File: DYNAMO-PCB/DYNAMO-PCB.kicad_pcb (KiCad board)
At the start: 2 copper layers, 39 parts, among them J1 HDMI_A, J10 Conn_01x03_Pin, J11 Conn_01x03_Pin, J12 Conn_01x03_Pin, J13 Conn_01x02_Pin, J17 USB3_A, J18 USB3_A, J19 USB3_A, J2 USB3_A, J20 USB3_A, J21 USB3_A, J22 USB3_A, J23 USB3_A, J24 USB3_A, J25 USB3_A, J26 USB_C_Receptacle_USB2.0_16P, J27 USB_C_Receptacle_USB2.0_16P, J28 USB_C_Receptacle_USB2.0_16P, J29 USB_C_Receptacle_USB2.0_16P, J3 Conn_01x03_Pin, J30 USB_C_Receptacle_USB2.0_16P, J31 USB_C_Receptacle_USB2.0_16P, J5 Conn_01x02_Pin, J6 Conn_01x03_Pin, J7 Conn_01x08_Socket, J8 Conn_01x03_Pin, J9 Conn_01x03_Pin, U2 CH7035B-BF

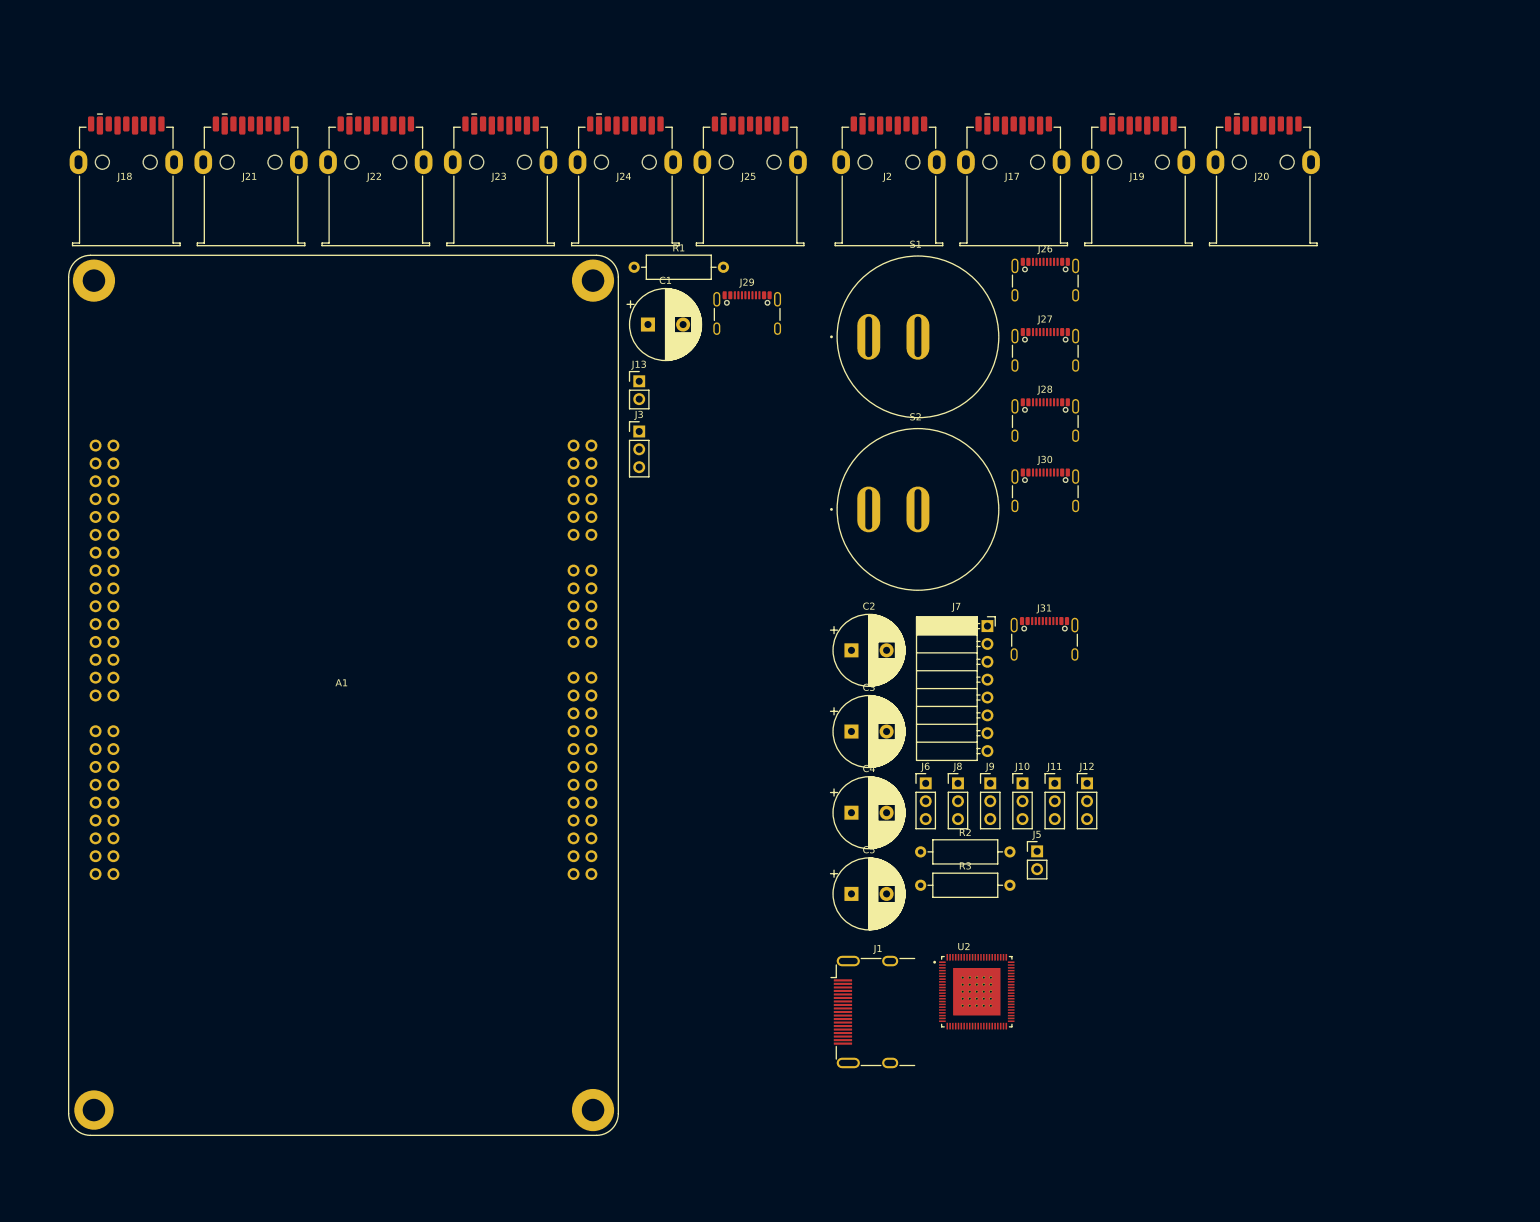
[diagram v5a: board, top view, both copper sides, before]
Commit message: wired headpcb sch
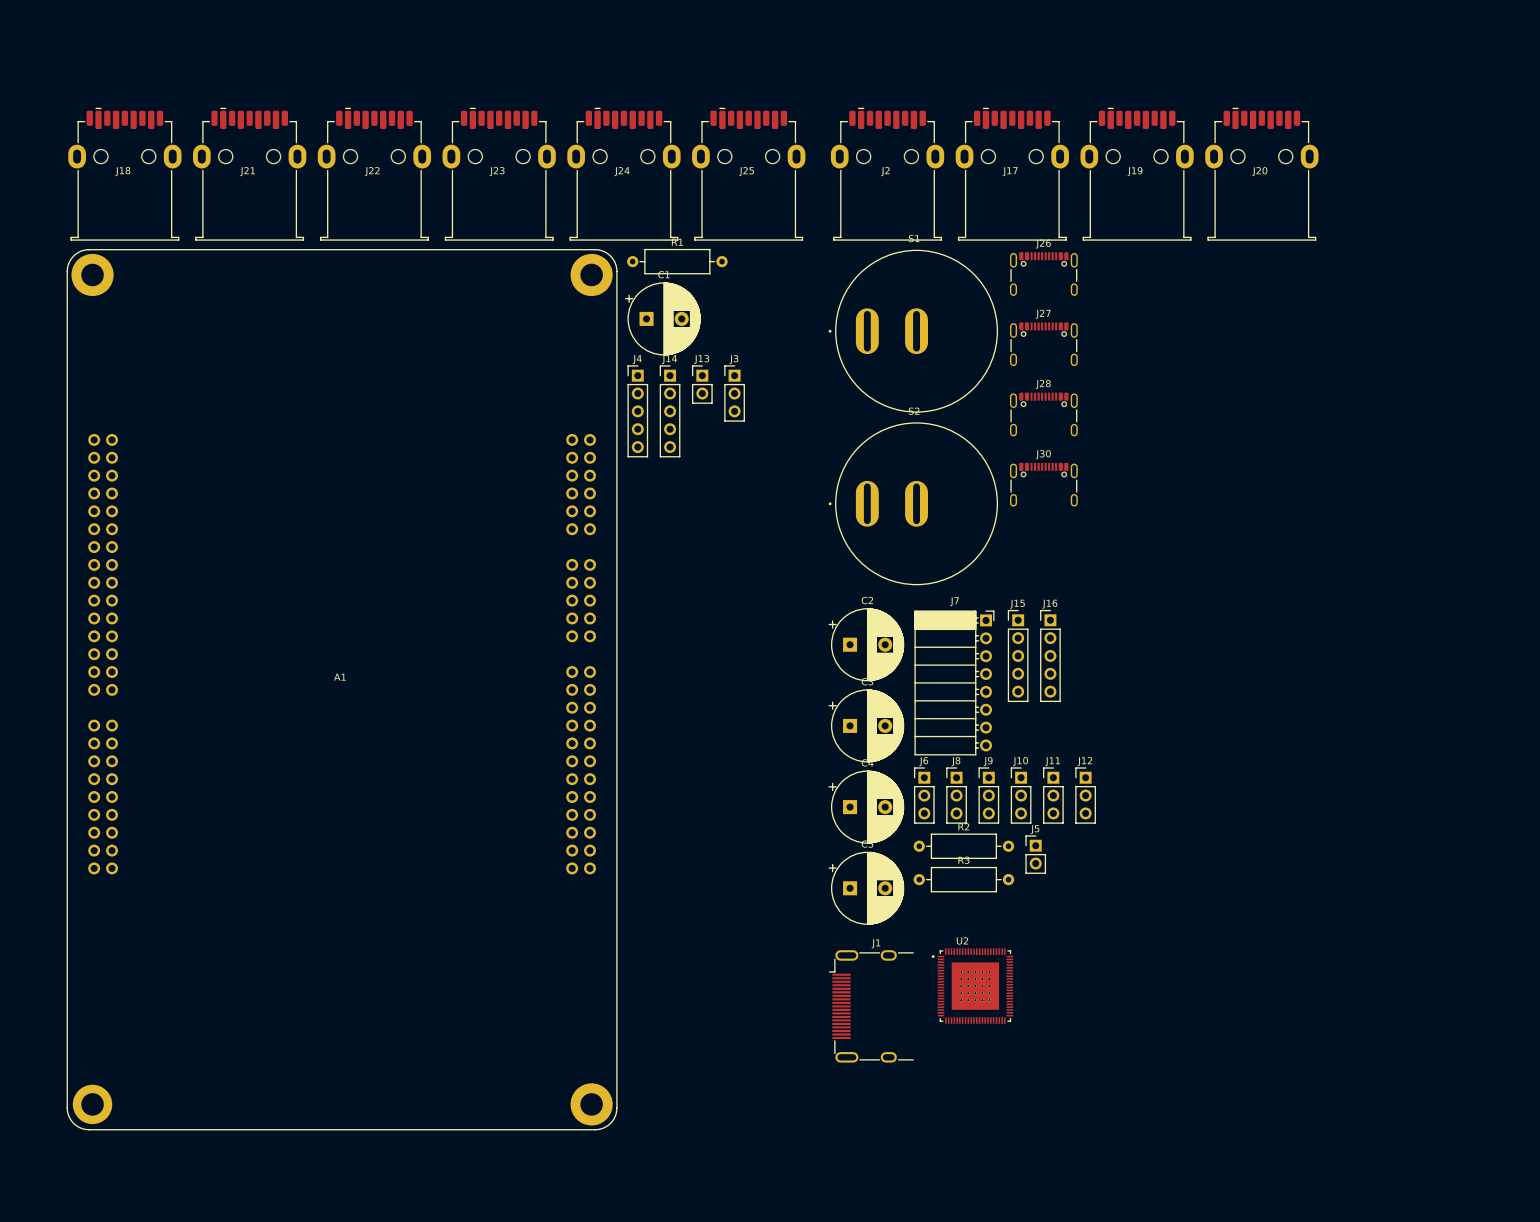
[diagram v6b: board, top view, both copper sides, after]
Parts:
- removed J29, J31: USB_C_Receptacle_USB2.0_16P, Connector_USB:USB_C_Receptacle_GCT_USB4105-xx-A_16P_TopMnt_Horizontal
- added J14: Conn_01x05_Pin, Connector_PinHeader_2.54mm:PinHeader_1x05_P2.54mm_Vertical, F.Cu at (137.8, 65.8)
- added J15: Conn_01x05_Pin, Connector_PinHeader_2.54mm:PinHeader_1x05_P2.54mm_Vertical, F.Cu at (187.3, 100.6)
- added J16: Conn_01x05_Pin, Connector_PinHeader_2.54mm:PinHeader_1x05_P2.54mm_Vertical, F.Cu at (191.9, 100.6)
- added J4: Conn_01x05_Pin, Connector_PinHeader_2.54mm:PinHeader_1x05_P2.54mm_Vertical, F.Cu at (133.2, 65.8)
- moved J3 15.7 mm to (146.9, 65.8)
- moved J13 9.02 mm to (142.4, 65.8)
- moved J5 0.82 mm to (189.8, 132.6)
- moved C3 0.82 mm to (163.4, 115.6)
- moved C5 0.82 mm to (163.4, 138.7)
- moved J7 0.82 mm to (182.7, 100.6)
- moved U2 0.82 mm to (181.2, 152.6)
- moved C1 0.82 mm to (134.4, 57.7)
- moved J12 0.82 mm to (196.9, 123.0)
- moved J17 0.82 mm to (186.3, 37.1)
- moved J19 0.82 mm to (204.0, 37.1)
- moved J2 0.82 mm to (168.5, 37.1)
- moved J20 0.82 mm to (221.8, 37.1)
- moved J24 0.82 mm to (131.0, 37.1)
- moved J25 0.82 mm to (148.8, 37.1)
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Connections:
- C2 pad 1: unconnected-(C2-Pad1) -> Net-(J10-Pin_2)
- C2 pad 2: unconnected-(C2-Pad2) -> Net-(J10-Pin_2)
- C3 pad 1: unconnected-(C3-Pad1) -> Net-(J10-Pin_2)
- C3 pad 2: unconnected-(C3-Pad2) -> Net-(J10-Pin_2)
- C4 pad 1: unconnected-(C4-Pad1) -> Net-(J10-Pin_2)
- C4 pad 2: unconnected-(C4-Pad2) -> Net-(J10-Pin_2)
- C5 pad 1: unconnected-(C5-Pad1) -> Net-(J10-Pin_2)
- C5 pad 2: unconnected-(C5-Pad2) -> Net-(J10-Pin_2)
- J10 pad 1: unconnected-(J10-Pin_1-Pad1) -> Net-(J10-Pin_1)
- J10 pad 2: unconnected-(J10-Pin_2-Pad2) -> Net-(J10-Pin_2)
- J10 pad 3: unconnected-(J10-Pin_3-Pad3) -> Net-(J10-Pin_2)
- J11 pad 1: unconnected-(J11-Pin_1-Pad1) -> Net-(J11-Pin_1)
- J11 pad 2: unconnected-(J11-Pin_2-Pad2) -> Net-(J10-Pin_2)
- J11 pad 3: unconnected-(J11-Pin_3-Pad3) -> Net-(J11-Pin_3)
- J12 pad 1: unconnected-(J12-Pin_1-Pad1) -> Net-(J12-Pin_1)
- J12 pad 2: unconnected-(J12-Pin_2-Pad2) -> Net-(J10-Pin_2)
- J12 pad 3: unconnected-(J12-Pin_3-Pad3) -> Net-(J11-Pin_3)
- J5 pad 1: unconnected-(J5-Pin_1-Pad1) -> Net-(J10-Pin_2)
- J5 pad 2: unconnected-(J5-Pin_2-Pad2) -> Net-(J11-Pin_3)
- J6 pad 1: unconnected-(J6-Pin_1-Pad1) -> Net-(J16-Pin_3)
- J6 pad 2: unconnected-(J6-Pin_2-Pad2) -> Net-(J10-Pin_2)
- J6 pad 3: unconnected-(J6-Pin_3-Pad3) -> Net-(J10-Pin_2)
- J7 pad 1: unconnected-(J7-Pin_1-Pad1) -> Net-(J10-Pin_2)
- J7 pad 2: unconnected-(J7-Pin_2-Pad2) -> Net-(J11-Pin_3)
- J7 pad 3: unconnected-(J7-Pin_3-Pad3) -> Net-(J15-Pin_4)
- J7 pad 4: unconnected-(J7-Pin_4-Pad4) -> Net-(J15-Pin_5)
- J8 pad 1: unconnected-(J8-Pin_1-Pad1) -> Net-(J16-Pin_4)
- J8 pad 2: unconnected-(J8-Pin_2-Pad2) -> Net-(J10-Pin_2)
- J8 pad 3: unconnected-(J8-Pin_3-Pad3) -> Net-(J10-Pin_2)
- J9 pad 1: unconnected-(J9-Pin_1-Pad1) -> Net-(J16-Pin_5)
- J9 pad 2: unconnected-(J9-Pin_2-Pad2) -> Net-(J10-Pin_2)
- J9 pad 3: unconnected-(J9-Pin_3-Pad3) -> Net-(J10-Pin_2)
- R2 pad 1: unconnected-(R2-Pad1) -> Net-(J15-Pin_2)
- R2 pad 2: unconnected-(R2-Pad2) -> Net-(J11-Pin_1)
- R3 pad 1: unconnected-(R3-Pad1) -> Net-(J15-Pin_1)
- R3 pad 2: unconnected-(R3-Pad2) -> Net-(J12-Pin_1)

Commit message: schematic wip
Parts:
- removed J14, J15, J16, J4: Conn_01x05_Pin, Connector_PinHeader_2.54mm:PinHeader_1x05_P2.54mm_Vertical
- added J29: USB_C_Receptacle_USB2.0_16P, Connector_USB:USB_C_Receptacle_GCT_USB4105-xx-A_16P_TopMnt_Horizontal, F.Cu at (185.0, 79.4)
- added J31: USB3_A, 692122030100:692122030100, F.Cu at (233.5, 34.2)
- added J32: USB3_A, 692122030100:692122030100, F.Cu at (251.3, 34.2)
- added J33: Conn_02x05_Counter_Clockwise, Connector_PinHeader_2.54mm:PinHeader_2x05_P2.54mm_Vertical, F.Cu at (181.3, 122.1)
- added J34: Conn_02x05_Counter_Clockwise, Connector_PinHeader_2.54mm:PinHeader_2x05_P2.54mm_Vertical, F.Cu at (127.2, 62.8)
- added S3: RR511D1121, RR511D1121:E-SWITCH_RR511D1121, F.Cu at (166.8, 105.5)
- moved J1 44.3 mm to (200.8, 128.8)
- moved U2 44.3 mm to (216.6, 126.0)
- moved C3 22.4 mm to (157.4, 137.2)
- moved J10 22.4 mm to (181.7, 144.5)
- moved J11 22.4 mm to (186.3, 144.5)
- moved J6 22.4 mm to (167.9, 144.5)
- moved J7 22.4 mm to (176.7, 122.2)
- moved J8 22.4 mm to (172.5, 144.5)
- moved J9 22.4 mm to (177.1, 144.5)
- moved J12 22.4 mm to (190.9, 144.5)
- moved C2 22.4 mm to (157.4, 125.6)
- moved C5 22.4 mm to (157.4, 160.2)
- moved R2 22.4 mm to (167.2, 154.3)
- moved R3 22.4 mm to (167.2, 159.0)
- moved J5 22.4 mm to (183.8, 154.2)
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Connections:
- C2 pad 2: Net-(J10-Pin_2) -> Net-(J10-Pin_3)
- C3 pad 2: Net-(J10-Pin_2) -> Net-(J10-Pin_3)
- C4 pad 2: Net-(J10-Pin_2) -> Net-(J10-Pin_3)
- C5 pad 2: Net-(J10-Pin_2) -> Net-(J10-Pin_3)
- J10 pad 3: Net-(J10-Pin_2) -> Net-(J10-Pin_3)
- J11 pad 3: Net-(J11-Pin_3) -> Net-(J10-Pin_3)
- J12 pad 3: Net-(J11-Pin_3) -> Net-(J10-Pin_3)
- J17 pad 1: unconnected-(J17-VBUS-Pad1) -> Net-(J17-VBUS)
- J17 pad 10: unconnected-(J17-SHIELD-Pad10) -> Net-(J17-SHIELD)
- J17 pad 4: unconnected-(J17-GND-Pad4) -> Net-(J17-GND)
- J19 pad 1: unconnected-(J19-VBUS-Pad1) -> Net-(J19-VBUS)
- J19 pad 10: unconnected-(J19-SHIELD-Pad10) -> Net-(J19-SHIELD)
- J19 pad 2: unconnected-(J19-D--Pad2) -> Net-(J19-D-)
- J19 pad 3: unconnected-(J19-D+-Pad3) -> Net-(J19-D+)
- J19 pad 4: unconnected-(J19-GND-Pad4) -> Net-(J17-GND)
- J19 pad 5: unconnected-(J19-SSRX--Pad5) -> Net-(J19-SSRX-)
- J19 pad 6: unconnected-(J19-SSRX+-Pad6) -> Net-(J19-SSRX+)
- J19 pad 7: unconnected-(J19-DRAIN-Pad7) -> Net-(J19-DRAIN)
- J19 pad 8: unconnected-(J19-SSTX--Pad8) -> Net-(J19-SSTX-)
- J19 pad 9: unconnected-(J19-SSTX+-Pad9) -> Net-(J19-SSTX+)
- J2 pad 1: unconnected-(J2-VBUS-Pad1) -> Net-(J17-VBUS)
- J2 pad 10: unconnected-(J2-SHIELD-Pad10) -> Net-(J17-SHIELD)
- J2 pad 4: unconnected-(J2-GND-Pad4) -> Net-(J17-GND)
- J20 pad 1: unconnected-(J20-VBUS-Pad1) -> Net-(J17-VBUS)
- J20 pad 10: unconnected-(J20-SHIELD-Pad10) -> Net-(J19-SHIELD)
- J20 pad 2: unconnected-(J20-D--Pad2) -> Net-(J19-D-)
- J20 pad 3: unconnected-(J20-D+-Pad3) -> Net-(J19-D+)
- J20 pad 4: unconnected-(J20-GND-Pad4) -> Net-(J17-GND)
- J20 pad 5: unconnected-(J20-SSRX--Pad5) -> Net-(J19-SSRX-)
- J20 pad 6: unconnected-(J20-SSRX+-Pad6) -> Net-(J19-SSRX+)
- J20 pad 7: unconnected-(J20-DRAIN-Pad7) -> Net-(J19-DRAIN)
- J20 pad 8: unconnected-(J20-SSTX--Pad8) -> Net-(J19-SSTX-)
- J20 pad 9: unconnected-(J20-SSTX+-Pad9) -> Net-(J19-SSTX+)
- J26 pad A5: unconnected-(J26-CC1-PadA5) -> Net-(J26-CC1)
- J26 pad B5: unconnected-(J26-CC2-PadB5) -> Net-(J26-CC2)
- J26 pad S1: unconnected-(J26-SHIELD-PadS1) -> Net-(J26-SHIELD)
- J27 pad A5: unconnected-(J27-CC1-PadA5) -> Net-(J27-CC1)
- J27 pad A6: unconnected-(J27-D+-PadA6) -> Net-(J27-D+-PadA6)
- J27 pad A7: unconnected-(J27-D--PadA7) -> Net-(J27-D--PadA7)
- J27 pad A8: unconnected-(J27-SBU1-PadA8) -> Net-(J27-SBU1)
- J27 pad B5: unconnected-(J27-CC2-PadB5) -> Net-(J27-CC2)
- J27 pad B6: unconnected-(J27-D+-PadB6) -> Net-(J27-D+-PadB6)
- J27 pad B7: unconnected-(J27-D--PadB7) -> Net-(J27-D--PadB7)
- J27 pad B8: unconnected-(J27-SBU2-PadB8) -> Net-(J27-SBU2)
- J27 pad S1: unconnected-(J27-SHIELD-PadS1) -> Net-(J27-SHIELD)
- J28 pad A1: Net-(J28-GND-PadA1) -> Net-(J26-GND-PadA1)
- J28 pad A12: Net-(J28-GND-PadA1) -> Net-(J26-GND-PadA1)
- J28 pad A5: unconnected-(J28-CC1-PadA5) -> Net-(J26-CC1)
- J28 pad A6: unconnected-(J28-D+-PadA6) -> Net-(J28-D+-PadA6)
- J28 pad A7: unconnected-(J28-D--PadA7) -> Net-(J28-D--PadA7)
- J28 pad A8: unconnected-(J28-SBU1-PadA8) -> Net-(J28-SBU1)
- J28 pad B1: Net-(J28-GND-PadA1) -> Net-(J26-GND-PadA1)
- J28 pad B12: Net-(J28-GND-PadA1) -> Net-(J26-GND-PadA1)
- J28 pad B5: unconnected-(J28-CC2-PadB5) -> Net-(J26-CC2)
- J28 pad B6: unconnected-(J28-D+-PadB6) -> Net-(J28-D+-PadB6)
- J28 pad B7: unconnected-(J28-D--PadB7) -> Net-(J28-D--PadB7)
- J28 pad B8: unconnected-(J28-SBU2-PadB8) -> Net-(J28-SBU2)
- J28 pad S1: unconnected-(J28-SHIELD-PadS1) -> Net-(J26-SHIELD)
- J30 pad A1: Net-(J30-GND-PadA1) -> Net-(J26-GND-PadA1)
- J30 pad A12: Net-(J30-GND-PadA1) -> Net-(J26-GND-PadA1)
- J30 pad A4: Net-(J30-VBUS-PadA4) -> Net-(J26-VBUS-PadA4)
- J30 pad A5: unconnected-(J30-CC1-PadA5) -> Net-(J26-CC1)
- J30 pad A6: unconnected-(J30-D+-PadA6) -> Net-(J28-D+-PadA6)
- J30 pad A7: unconnected-(J30-D--PadA7) -> Net-(J28-D--PadA7)
- J30 pad A8: unconnected-(J30-SBU1-PadA8) -> Net-(J28-SBU1)
- J30 pad A9: Net-(J30-VBUS-PadA4) -> Net-(J26-VBUS-PadA4)
- J30 pad B1: Net-(J30-GND-PadA1) -> Net-(J26-GND-PadA1)
- J30 pad B12: Net-(J30-GND-PadA1) -> Net-(J26-GND-PadA1)
- J30 pad B4: Net-(J30-VBUS-PadA4) -> Net-(J26-VBUS-PadA4)
- J30 pad B5: unconnected-(J30-CC2-PadB5) -> Net-(J26-CC2)
- J30 pad B6: unconnected-(J30-D+-PadB6) -> Net-(J28-D+-PadB6)
- J30 pad B7: unconnected-(J30-D--PadB7) -> Net-(J28-D--PadB7)
- J30 pad B8: unconnected-(J30-SBU2-PadB8) -> Net-(J28-SBU2)
- J30 pad B9: Net-(J30-VBUS-PadA4) -> Net-(J26-VBUS-PadA4)
- J30 pad S1: unconnected-(J30-SHIELD-PadS1) -> Net-(J26-SHIELD)
- J5 pad 2: Net-(J11-Pin_3) -> Net-(J10-Pin_3)
- J6 pad 3: Net-(J10-Pin_2) -> Net-(J10-Pin_3)
- J7 pad 2: Net-(J11-Pin_3) -> Net-(J10-Pin_3)
- J8 pad 3: Net-(J10-Pin_2) -> Net-(J10-Pin_3)
- J9 pad 3: Net-(J10-Pin_2) -> Net-(J10-Pin_3)
- S1 pad 1: unconnected-(S1-Pad1) -> Net-(J17-VBUS)
- S1 pad 2: unconnected-(S1-Pad2) -> Net-(J19-VBUS)
- S2 pad 1: unconnected-(S2-Pad1) -> Net-(J28-VBUS-PadA4)
- S2 pad 2: unconnected-(S2-Pad2) -> Net-(J26-VBUS-PadA4)
